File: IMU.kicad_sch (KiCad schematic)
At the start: 1 part, among them U3 4754

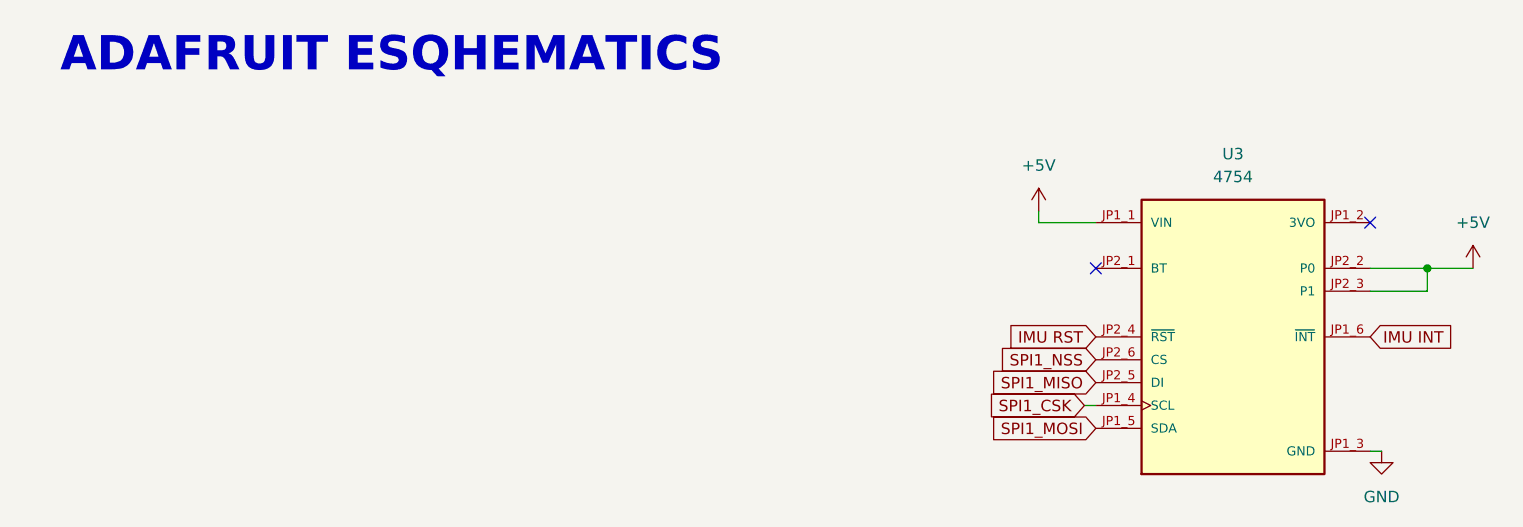
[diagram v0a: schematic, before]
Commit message: Actualización de nets
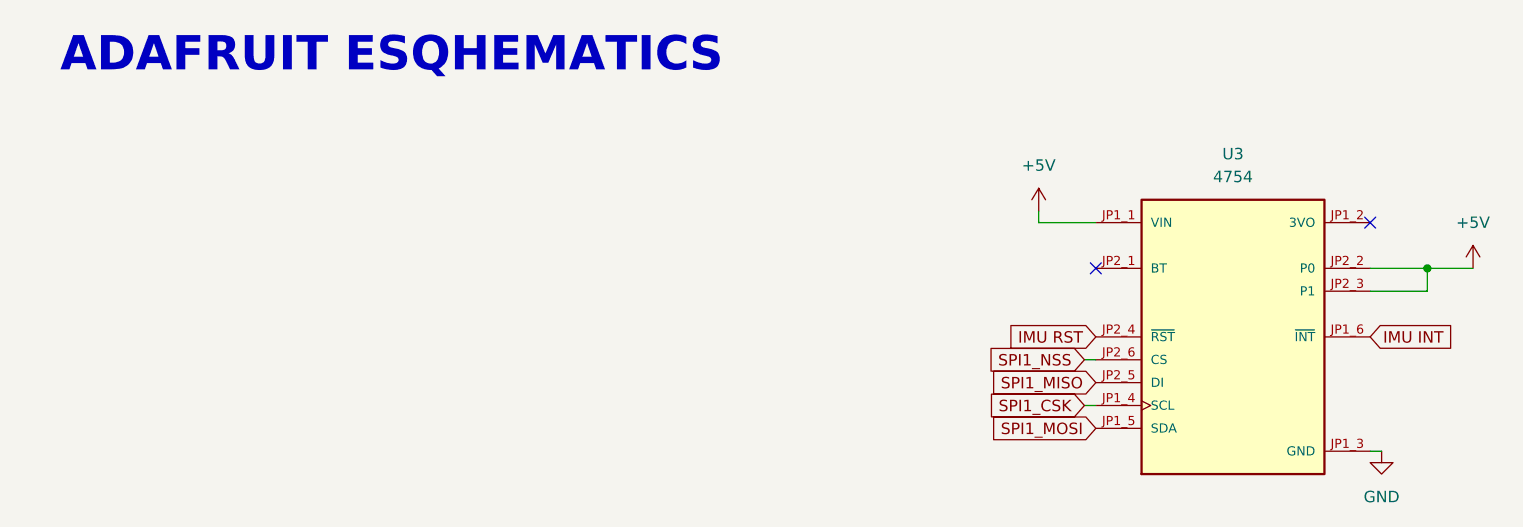
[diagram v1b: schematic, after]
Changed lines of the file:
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@@
 	(wire
 		(pts
+			(xy 148.59 110.49) (xy 149.86 110.49)
+		)
+		(stroke
+			(width 0)
+			(type default)
+		)
+	)
+	(wire
+		(pts
 			(xy 180.34 120.65) (xy 181.61 120.65)
 		)
@@
 	)
 	(image
-		(at 241.3 40.64)
+		(at 167.64 69.85)
 		(data "iVBORw0KGgoAAAANSUhEUgAAAf0AAAE7CAYAAADXfVghAAAABHNCSVQICAgIfAhkiAAAIABJREFU"
 			"eJzs3Xd8VFX6P/DP9EnvlVQSCCEkEBIgoUOoErCholh++NX1q+u6rquo2HBVQBd3X7ZVV0TFguJX"
@@
 	(global_label "SPI1_NSS"
 		(shape input)
-		(at 149.86 110.49 180)
+		(at 148.59 110.49 180)
 		(fields_autoplaced yes)
 		(effects
@@
 		)
 		(property "Intersheetrefs" "${INTERSHEET_REFS}"
-			(at 137.8639 110.49 0)
+			(at 136.5939 110.49 0)
 			(hide yes)
 			(show_name no)

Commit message: Arreglando footprints
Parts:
- renumbered U3 to U2
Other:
- company: (none) -> TOMEK TEAM
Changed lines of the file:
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@@
 	(generator_version "10.0")
 	(paper "A4")
+	(title_block
+		(company "TOMEK TEAM")
+	)
 	(text "ADAFRUIT ESQHEMATICS\n"
 		(exclude_from_sim no)
@@
 		(dnp no)
 		(fields_autoplaced yes)
-		(property "Reference" "#PWR050"
+		(property "Reference" "#PWR028"
 			(at 143.51 97.79 0)
 			(hide yes)
@@
 			(project "ARLISS_STM32_2026"
 				(path "/9719ea46-14c4-4409-9c57-49dd5454c03f/243e1b39-32df-463e-8f3d-bc06fe39ea80"
-					(reference "#PWR050")
+					(reference "#PWR028")
 					(unit 1)
 				)
@@
 		(dnp no)
 		(fields_autoplaced yes)
-		(property "Reference" "U3"
+		(property "Reference" "U2"
 			(at 165.1 87.63 0)
 			(show_name no)
@@
 			(project "ARLISS_STM32_2026"
 				(path "/9719ea46-14c4-4409-9c57-49dd5454c03f/243e1b39-32df-463e-8f3d-bc06fe39ea80"
-					(reference "U3")
+					(reference "U2")
 					(unit 1)
 				)
@@
 		(dnp no)
 		(fields_autoplaced yes)
-		(property "Reference" "#PWR051"
+		(property "Reference" "#PWR029"
 			(at 181.61 127 0)
 			(hide yes)
@@
 			(project "ARLISS_STM32_2026"
 				(path "/9719ea46-14c4-4409-9c57-49dd5454c03f/243e1b39-32df-463e-8f3d-bc06fe39ea80"
-					(reference "#PWR051")
+					(reference "#PWR029")
 					(unit 1)
 				)
@@
 		(dnp no)
 		(fields_autoplaced yes)
-		(property "Reference" "#PWR052"
+		(property "Reference" "#PWR030"
 			(at 191.77 104.14 0)
 			(hide yes)
@@
 			(project "ARLISS_STM32_2026"
 				(path "/9719ea46-14c4-4409-9c57-49dd5454c03f/243e1b39-32df-463e-8f3d-bc06fe39ea80"
-					(reference "#PWR052")
+					(reference "#PWR030")
 					(unit 1)
 				)

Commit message: Todo antes de PCB
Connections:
- net +5V renamed +3.3V
- net SPI1_CSK renamed SPI1_SCLK
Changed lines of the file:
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@@
 		(color 0 0 0 0)
 	)
+	(junction
+		(at 143.51 95.25)
+		(diameter 0)
+		(color 0 0 0 0)
+	)
 	(no_connect
 		(at 180.34 95.25)
@@
 		)
 	)
-	(global_label "SPI1_CSK"
+	(global_label "SPI1_SCLK"
 		(shape input)
 		(at 148.59 115.57 180)
@@
 		)
 		(property "Intersheetrefs" "${INTERSHEET_REFS}"
-			(at 136.5939 115.57 0)
+			(at 135.5658 115.57 0)
 			(hide yes)
 			(show_name no)
@@
 	)
 	(symbol
-		(lib_id "power:+5V")
-		(at 143.51 93.98 0)
-		(unit 1)
-		(body_style 1)
-		(exclude_from_sim no)
-		(in_bom yes)
-		(on_board yes)
-		(in_pos_files yes)
-		(dnp no)
-		(fields_autoplaced yes)
-		(property "Reference" "#PWR028"
-			(at 143.51 97.79 0)
-			(hide yes)
-			(show_name no)
-			(do_not_autoplace no)
-			(effects
-				(font
-					(size 1.27 1.27)
-				)
-			)
-		)
-		(property "Value" "+5V"
-			(at 143.51 88.9 0)
-			(show_name no)
-			(do_not_autoplace no)
-			(effects
-				(font
-					(size 1.27 1.27)
-				)
-			)
-		)
-		(property "Footprint" ""
-			(at 143.51 93.98 0)
-			(hide yes)
-			(show_name no)
-			(do_not_autoplace no)
-			(effects
-				(font
-					(size 1.27 1.27)
-				)
-			)
-		)
-		(property "Datasheet" ""
-			(at 143.51 93.98 0)
-			(hide yes)
-			(show_name no)
-			(do_not_autoplace no)
-			(effects
-				(font
-					(size 1.27 1.27)
-				)
-			)
-		)
-		(property "Description" "Power symbol creates a global label with name \"+5V\""
-			(at 143.51 93.98 0)
-			(hide yes)
-			(show_name no)
-			(do_not_autoplace no)
-			(effects
-				(font
-					(size 1.27 1.27)
-				)
-			)
-		)
-		(pin "1"
-		)
-		(instances
-			(project "ARLISS_STM32_2026"
-				(path "/9719ea46-14c4-4409-9c57-49dd5454c03f/243e1b39-32df-463e-8f3d-bc06fe39ea80"
-					(reference "#PWR028")
-					(unit 1)
-				)
-			)
-		)
-	)
-	(symbol
 		(lib_id "4754:4754")
 		(at 165.1 107.95 0)
@@
 			(at 165.1 107.95 0)
 			(hide yes)
-			(show_name no)
+			(show_name yes)
 			(do_not_autoplace no)
 			(effects
@@
 	)
 	(symbol
-		(lib_id "power:+5V")
+		(lib_id "power:+3.3V")
+		(at 143.51 93.98 0)
+		(unit 1)
+		(body_style 1)
+		(exclude_from_sim no)
+		(in_bom yes)
+		(on_board yes)
+		(in_pos_files yes)
+		(dnp no)
+		(fields_autoplaced yes)
+		(property "Reference" "#PWR028"
+			(at 143.51 97.79 0)
+			(hide yes)
+			(show_name no)
+			(do_not_autoplace no)
+			(effects
+				(font
+					(size 1.27 1.27)
+				)
+			)
+		)
+		(property "Value" "+3.3V"
+			(at 143.51 88.9 0)
+			(show_name no)
+			(do_not_autoplace no)
+			(effects
+				(font
+					(size 1.27 1.27)
+				)
+			)
+		)
+		(property "Footprint" ""
+			(at 143.51 93.98 0)
+			(hide yes)
+			(show_name no)
+			(do_not_autoplace no)
+			(effects
+				(font
+					(size 1.27 1.27)
+				)
+			)
+		)
+		(property "Datasheet" ""
+			(at 143.51 93.98 0)
+			(hide yes)
+			(show_name no)
+			(do_not_autoplace no)
+			(effects
+				(font
+					(size 1.27 1.27)
+				)
+			)
+		)
+		(property "Description" "Power symbol creates a global label with name \"+3.3V\""
+			(at 143.51 93.98 0)
+			(hide yes)
+			(show_name no)
+			(do_not_autoplace no)
+			(effects
+				(font
+					(size 1.27 1.27)
+				)
+			)
+		)
+		(pin "1"
+		)
+		(instances
+			(project "ARLISS_STM32_2026"
+				(path "/9719ea46-14c4-4409-9c57-49dd5454c03f/243e1b39-32df-463e-8f3d-bc06fe39ea80"
+					(reference "#PWR028")
+					(unit 1)
+				)
+			)
+		)
+	)
+	(symbol
+		(lib_id "power:PWR_FLAG")
+		(at 143.51 95.25 180)
+		(unit 1)
+		(body_style 1)
+		(exclude_from_sim no)
+		(in_bom yes)
+		(on_board yes)
+		(in_pos_files yes)
+		(dnp no)
+		(fields_autoplaced yes)
+		(property "Reference" "#FLG01"
+			(at 143.51 97.155 0)
+			(hide yes)
+			(show_name no)
+			(do_not_autoplace no)
+			(effects
+				(font
+					(size 1.27 1.27)
+				)
+			)
+		)
+		(property "Value" "PWR_FLAG"
+			(at 143.51 100.33 0)
+			(show_name no)
+			(do_not_autoplace no)
+			(effects
+				(font
+					(size 1.27 1.27)
+				)
+			)
+		)
+		(property "Footprint" ""
+			(at 143.51 95.25 0)
+			(hide yes)
+			(show_name no)
+			(do_not_autoplace no)
+			(effects
+				(font
+					(size 1.27 1.27)
+				)
+			)
+		)
+		(property "Datasheet" ""
+			(at 143.51 95.25 0)
+			(hide yes)
+			(show_name no)
+			(do_not_autoplace no)
+			(effects
+				(font
+					(size 1.27 1.27)
+				)
+			)
+		)
+		(property "Description" "Special symbol for telling ERC where power comes from"
+			(at 143.51 95.25 0)
+			(hide yes)
+			(show_name no)
+			(do_not_autoplace no)
+			(effects
+				(font
+					(size 1.27 1.27)
+				)
+			)
+		)
+		(pin "1"
+		)
+		(instances
+			(project "ARLISS_STM32_2026"
+				(path "/9719ea46-14c4-4409-9c57-49dd5454c03f/243e1b39-32df-463e-8f3d-bc06fe39ea80"
+					(reference "#FLG01")
+					(unit 1)
+				)
+			)
+		)
+	)
+	(symbol
+		(lib_id "power:+3.3V")
 		(at 191.77 100.33 0)
 		(unit 1)
@@
 			)
 		)
-		(property "Value" "+5V"
+		(property "Value" "+3.3V"
 			(at 191.77 95.25 0)
 			(show_name no)
@@
 			)
 		)
-		(property "Description" "Power symbol creates a global label with name \"+5V\""
+		(property "Description" "Power symbol creates a global label with name \"+3.3V\""
 			(at 191.77 100.33 0)
 			(hide yes)
